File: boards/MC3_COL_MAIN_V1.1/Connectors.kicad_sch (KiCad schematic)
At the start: 11 parts, among them J13 HARNESS_FFC_6P, J3 ENC_leaf1, J4 ENC_leaf2, J5 ENC_leaf3, J6 ENC_leaf4

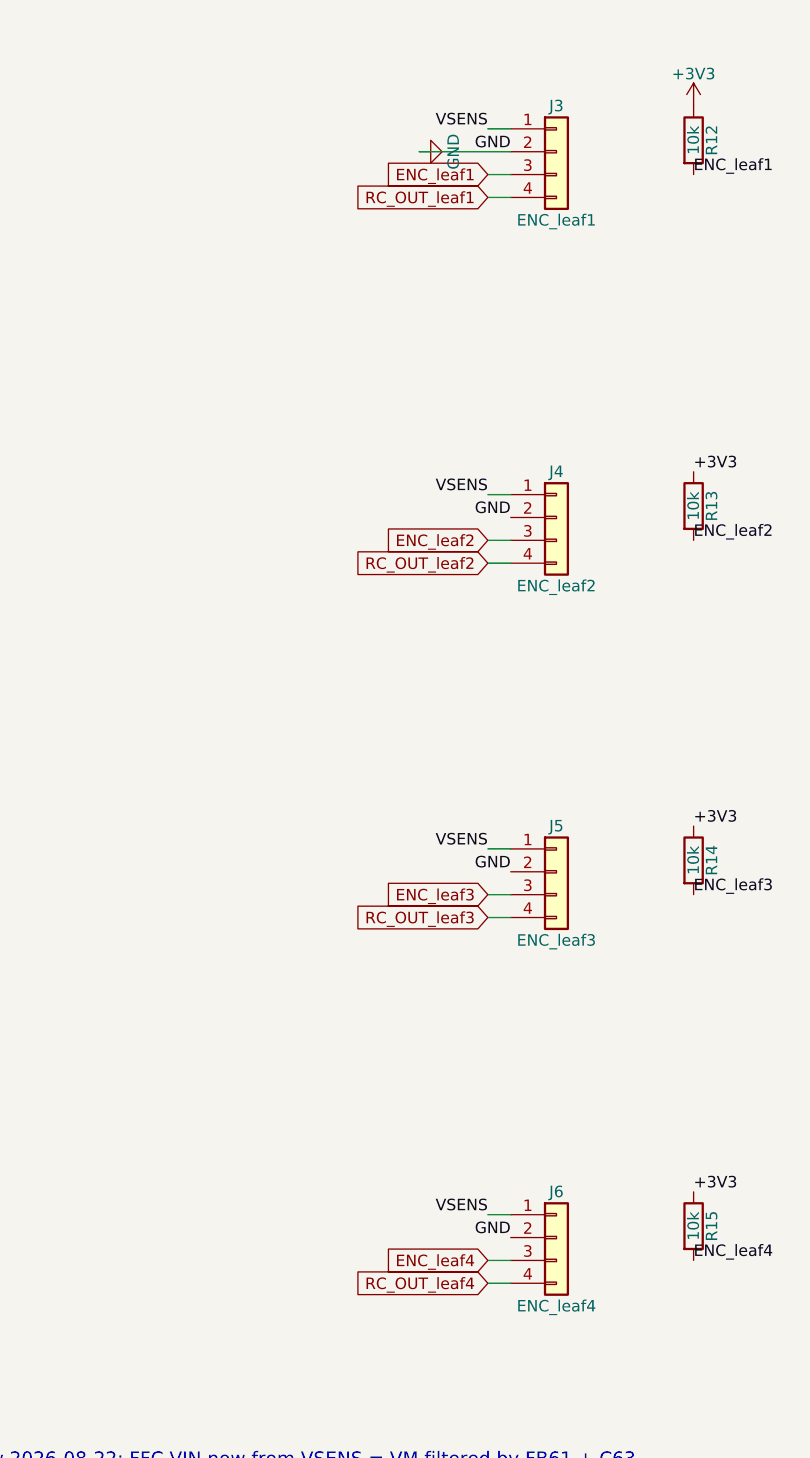
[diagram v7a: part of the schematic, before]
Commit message: V1.1: encoder connector nets swapped to match placement (J3=leaf2, J4=leaf1, J5=leaf4, J6=leaf3)
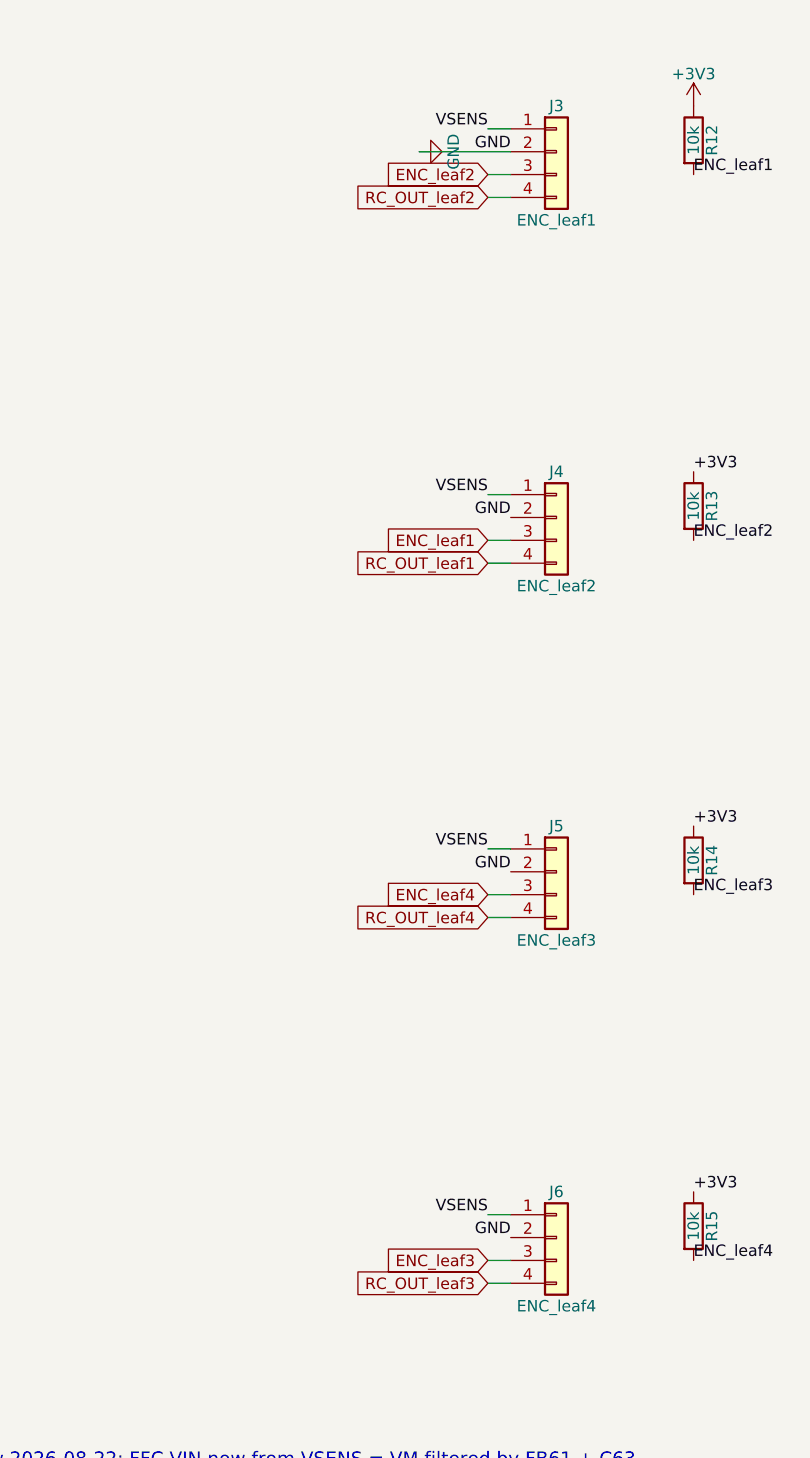
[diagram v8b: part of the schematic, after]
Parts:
- J3: Note Encoder FFC leaf1. Pin 4 (spare) wired to RC_OUT_leaf1 (202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 -> Encoder FFC leaf2 (net swap 2026-08-27: this connector sits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
- J4: Note Encoder FFC leaf2. Pin 4 -> RC_OUT_leaf2, dual-mode fallbac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 -> Encoder FFC leaf1 (net swap 2026-08-27: beside leaf1's moto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
- J5: Note Encoder FFC leaf3. Pin 4 -> RC_OUT_leaf3, dual-mode fallbac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 -> Encoder FFC leaf4 (net swap 2026-08-27: beside leaf4's moto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
- J6: Note Encoder FFC leaf4. Pin 4 -> RC_OUT_leaf4, dual-mode fallbac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 -> Encoder FFC leaf3 (net swap 2026-08-27: beside leaf3's moto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
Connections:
- net ENC_leaf1: now also J4.3 (Pin_3); no longer J3.3 (Pin_3)
- net ENC_leaf2: now also J3.3 (Pin_3); no longer J4.3 (Pin_3)
- net ENC_leaf3: now also J6.3 (Pin_3); no longer J5.3 (Pin_3)
- net ENC_leaf4: now also J5.3 (Pin_3); no longer J6.3 (Pin_3)
- net RC_OUT_leaf1: now also J4.4 (Pin_4); no longer J3.4 (Pin_4)
- net RC_OUT_leaf2: now also J3.4 (Pin_4); no longer J4.4 (Pin_4)
- net RC_OUT_leaf3: now also J6.4 (Pin_4); no longer J5.4 (Pin_4)
- net RC_OUT_leaf4: now also J5.4 (Pin_4); no longer J6.4 (Pin_4)
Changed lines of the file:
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@@
+	(wire
+		(pts
+			(xy 54.61 175.26)
+			(xy 52.07 175.26)
+		)
+		(stroke
+			(width 0)
+			(type default)
+		)
+	)
 	(wire
 		(pts
@@
 	(wire
 		(pts
+			(xy 54.61 134.62)
+			(xy 52.07 134.62)
+		)
+		(stroke
+			(width 0)
+			(type default)
+		)
+	)
+	(wire
+		(pts
 			(xy 54.61 87.63)
 			(xy 52.07 87.63)
@@
 	(wire
 		(pts
+			(xy 54.61 54.61)
+			(xy 52.07 54.61)
+		)
+		(stroke
+			(width 0)
+			(type default)
+		)
+	)
+	(wire
+		(pts
 			(xy 147.32 63.5)
 			(xy 144.78 63.5)
@@
 	(wire
 		(pts
+			(xy 54.61 95.25)
+			(xy 52.07 95.25)
+		)
+		(stroke
+			(width 0)
+			(type default)
+		)
+	)
+	(wire
+		(pts
 			(xy 54.61 172.72)
 			(xy 52.07 172.72)
@@
 			(width 0)
 			(type default)
-		)
-	)
-	(wire
-		(pts
-			(xy 54.61 54.61)
-			(xy 52.07 54.61)
-		)
-	)
-	(wire
-		(pts
-			(xy 54.61 95.25)
-			(xy 52.07 95.25)
-		)
-	)
-	(wire
-		(pts
-			(xy 54.61 134.62)
-			(xy 52.07 134.62)
-		)
-	)
-	(wire
-		(pts
-			(xy 54.61 175.26)
-			(xy 52.07 175.26)
 		)
 	)
@@
 		)
 	)
-	(global_label "ENC_leaf2"
-		(shape input)
-		(at 52.07 92.71 180)
-		(effects
-			(font
-				(size 1.27 1.27)
-			)
-			(justify right)
-		)
-		(property "Intersheetrefs" "${INTERSHEET_REFS}"
-			(at 52.07 92.71 0)
-			(hide yes)
-			(show_name no)
-			(do_not_autoplace no)
-			(effects
-				(font
-					(size 1.27 1.27)
-				)
-			)
-		)
-	)
-	(global_label "ENC_leaf1"
-		(shape input)
-		(at 52.07 52.07 180)
-		(effects
-			(font
-				(size 1.27 1.27)
-			)
-			(justify right)
-		)
-		(property "Intersheetrefs" "${INTERSHEET_REFS}"
-			(at 52.07 52.07 0)
-			(hide yes)
-			(show_name no)
-			(do_not_autoplace no)
-			(effects
-				(font
-					(size 1.27 1.27)
-				)
-			)
-		)
-	)
 	(global_label "YAW_OUT1"
 		(shape input)
@@
 		)
 	)
+	(global_label "ENC_leaf2"
+		(shape input)
+		(at 52.07 52.07 180)
+		(effects
+			(font
+				(size 1.27 1.27)
+			)
+			(justify right)
+		)
+	)
+	(global_label "RC_OUT_leaf2"
+		(shape input)
+		(at 52.07 54.61 180)
+		(effects
+			(font
+				(size 1.27 1.27)
+			)
+			(justify right)
+		)
+	)
+	(global_label "ENC_leaf1"
+		(shape input)
+		(at 52.07 92.71 180)
+		(effects
+			(font
+				(size 1.27 1.27)
+			)
+			(justify right)
+		)
+	)
+	(global_label "RC_OUT_leaf1"
+		(shape input)
+		(at 52.07 95.25 180)
+		(effects
+			(font
+				(size 1.27 1.27)
+			)
+			(justify right)
+		)
+	)
+	(global_label "ENC_leaf4"
+		(shape input)
+		(at 52.07 132.08 180)
+		(effects
+			(font
+				(size 1.27 1.27)
+			)
+			(justify right)
+		)
+	)
+	(global_label "RC_OUT_leaf4"
+		(shape input)
+		(at 52.07 134.62 180)
+		(effects
+			(font
+				(size 1.27 1.27)
+			)
+			(justify right)
+		)
+	)
 	(global_label "ENC_leaf3"
 		(shape input)
-		(at 52.07 132.08 180)
+		(at 52.07 172.72 180)
 		(effects
 			(font
@@
 			(justify right)
 		)
-		(property "Intersheetrefs" "${INTERSHEET_REFS}"
-			(at 52.07 132.08 0)
-			(hide yes)
-			(show_name no)
-			(do_not_autoplace no)
-			(effects
-				(font
-					(size 1.27 1.27)
-				)
-			)
-		)
-	)
-	(global_label "ENC_leaf4"
-		(shape input)
-		(at 52.07 172.72 180)
-		(effects
-			(font
-				(size 1.27 1.27)
-			)
-			(justify right)
-		)
-		(property "Intersheetrefs" "${INTERSHEET_REFS}"
-			(at 52.07 172.72 0)
-			(hide yes)
-			(show_name no)
-			(do_not_autoplace no)
-			(effects
-				(font
-					(size 1.27 1.27)
-				)
-			)
-		)
-	)
-	(global_label "RC_OUT_leaf1"
-		(shape input)
-		(at 52.07 54.61 180)
-		(effects
-			(font
-				(size 1.27 1.27)
-			)
-			(justify right)
-		)
-	)
-	(global_label "RC_OUT_leaf2"
-		(shape input)
-		(at 52.07 95.25 180)
-		(effects
-			(font
-				(size 1.27 1.27)
-			)
-			(justify right)
-		)
 	)
 	(global_label "RC_OUT_leaf3"
-		(shape input)
-		(at 52.07 134.62 180)
-		(effects
-			(font
-				(size 1.27 1.27)
-			)
-			(justify right)
-		)
-	)
-	(global_label "RC_OUT_leaf4"
 		(shape input)
 		(at 52.07 175.26 180)
@@
 			)
 		)
-		(property "Note" "Encoder FFC leaf1. Pin 4 (spare) wired to RC_OUT_leaf1 (2026-08-27): dual-mode fallback - with the inductive board the pin floats at the far end and the DRV8214 ripple counter owns the net (open-drain); with an AEDR-8300 optical fallback board its B channel drives the net and firmware sets DIS_EC so the DRV releases it. A on pin 3 as before. See Main-Board-01 Encoder Interface s Optical Fallback."
+		(property "Note" "Encoder FFC leaf2 (net swap 2026-08-27: this connector sits beside leaf2's motor pads J8). Pin 3 ENC_leaf2, pin 4 RC_OUT_leaf2 - dual-mode optical fallback, see Main-Board-01 Encoder Interface s Optical Fallback."
 			(at 59.69 49.53 0)
 			(hide yes)
@@
 			)
 		)
-		(property "Note" "Encoder FFC leaf4. Pin 4 -> RC_OUT_leaf4, dual-mode fallback - see J3."
+		(property "Note" "Encoder FFC leaf3 (net swap 2026-08-27: beside leaf3's motor pads J9). Pin 3 ENC_leaf3, pin 4 RC_OUT_leaf3 - dual-mode optical fallback, see J3."
 			(at 59.69 170.18 0)
 			(hide yes)
@@
 			)
 		)
-		(property "Note" "Encoder FFC leaf2. Pin 4 -> RC_OUT_leaf2, dual-mode fallback - see J3."
+		(property "Note" "Encoder FFC leaf1 (net swap 2026-08-27: beside leaf1's motor pads J7). Pin 3 ENC_leaf1, pin 4 RC_OUT_leaf1 - dual-mode optical fallback, see J3."
 			(at 59.69 90.17 0)
 			(hide yes)
@@
 			)
 		)
-		(property "Note" "Encoder FFC leaf3. Pin 4 -> RC_OUT_leaf3, dual-mode fallback - see J3."
+		(property "Note" "Encoder FFC leaf4 (net swap 2026-08-27: beside leaf4's motor pads J10). Pin 3 ENC_leaf4, pin 4 RC_OUT_leaf4 - dual-mode optical fallback, see J3."
 			(at 59.69 129.54 0)
 			(hide yes)
